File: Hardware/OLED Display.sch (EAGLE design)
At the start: 16 parts, among them J1 SM04B-SRSS-TB, J2 SM04B-SRSS-TB, U1 QG-2832TLBFG02, U2 APX803

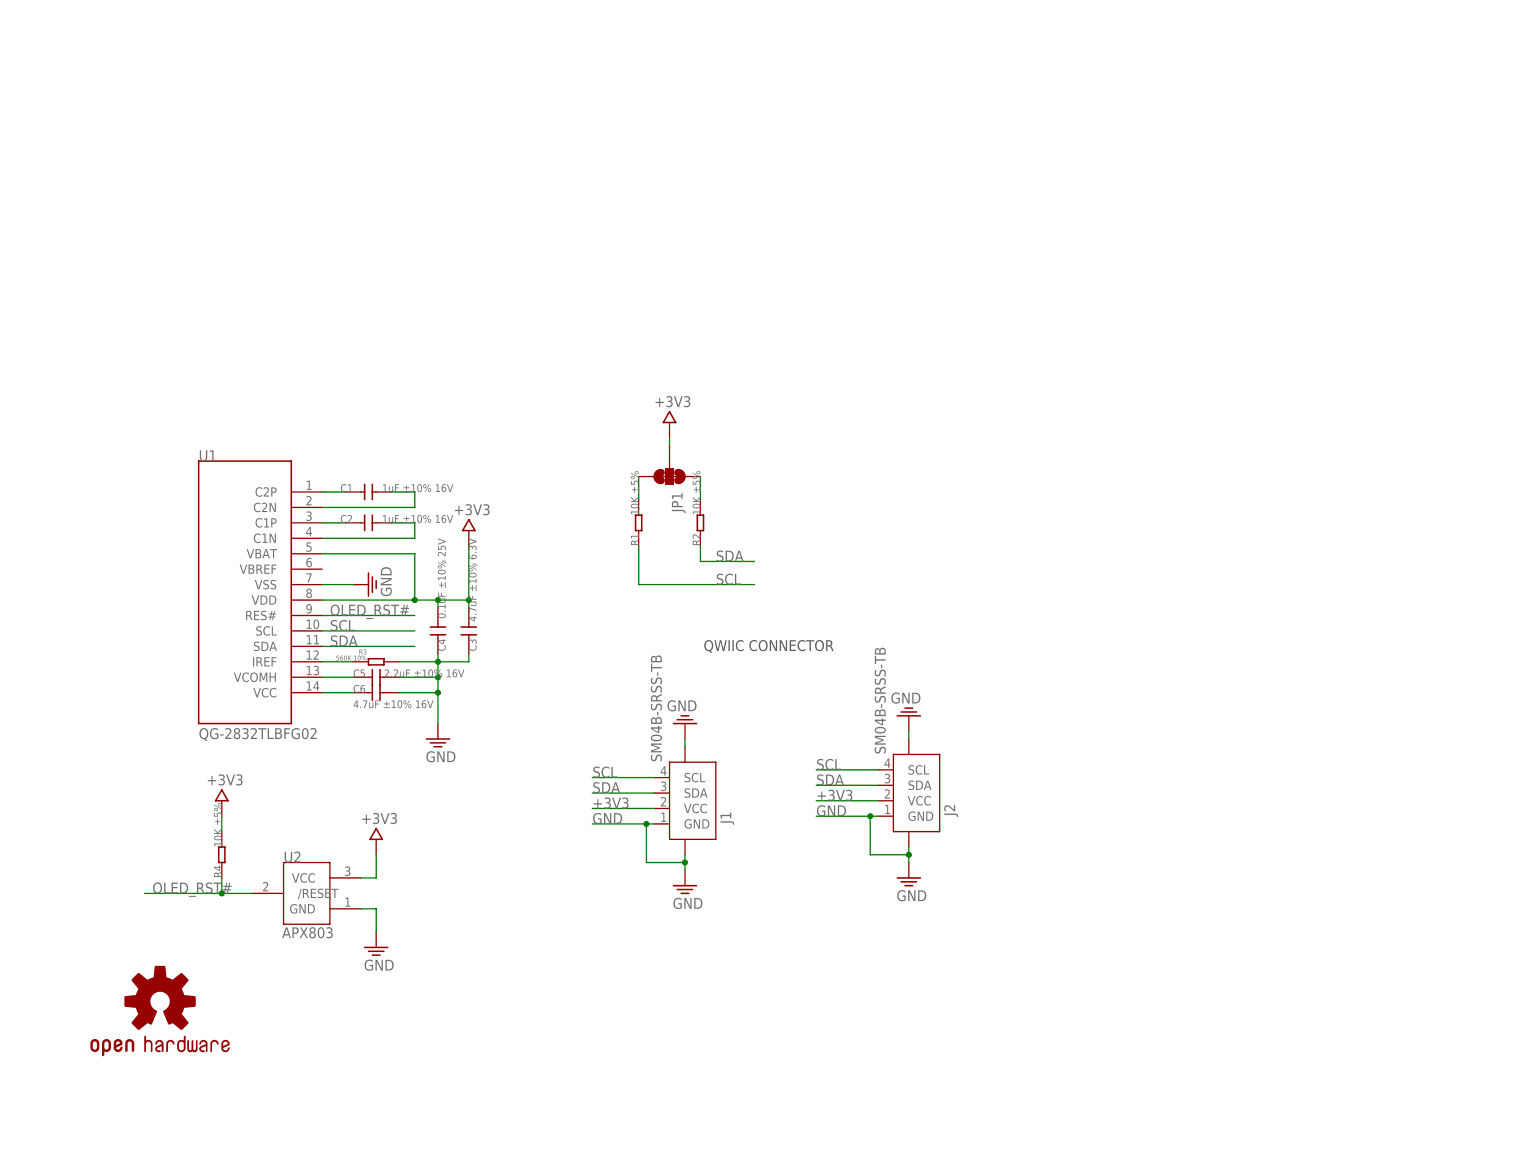
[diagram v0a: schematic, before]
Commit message: Replaces parts not in the SparkFun Eagle Libraries, adds logos, moves qwiic connectors and standoffs
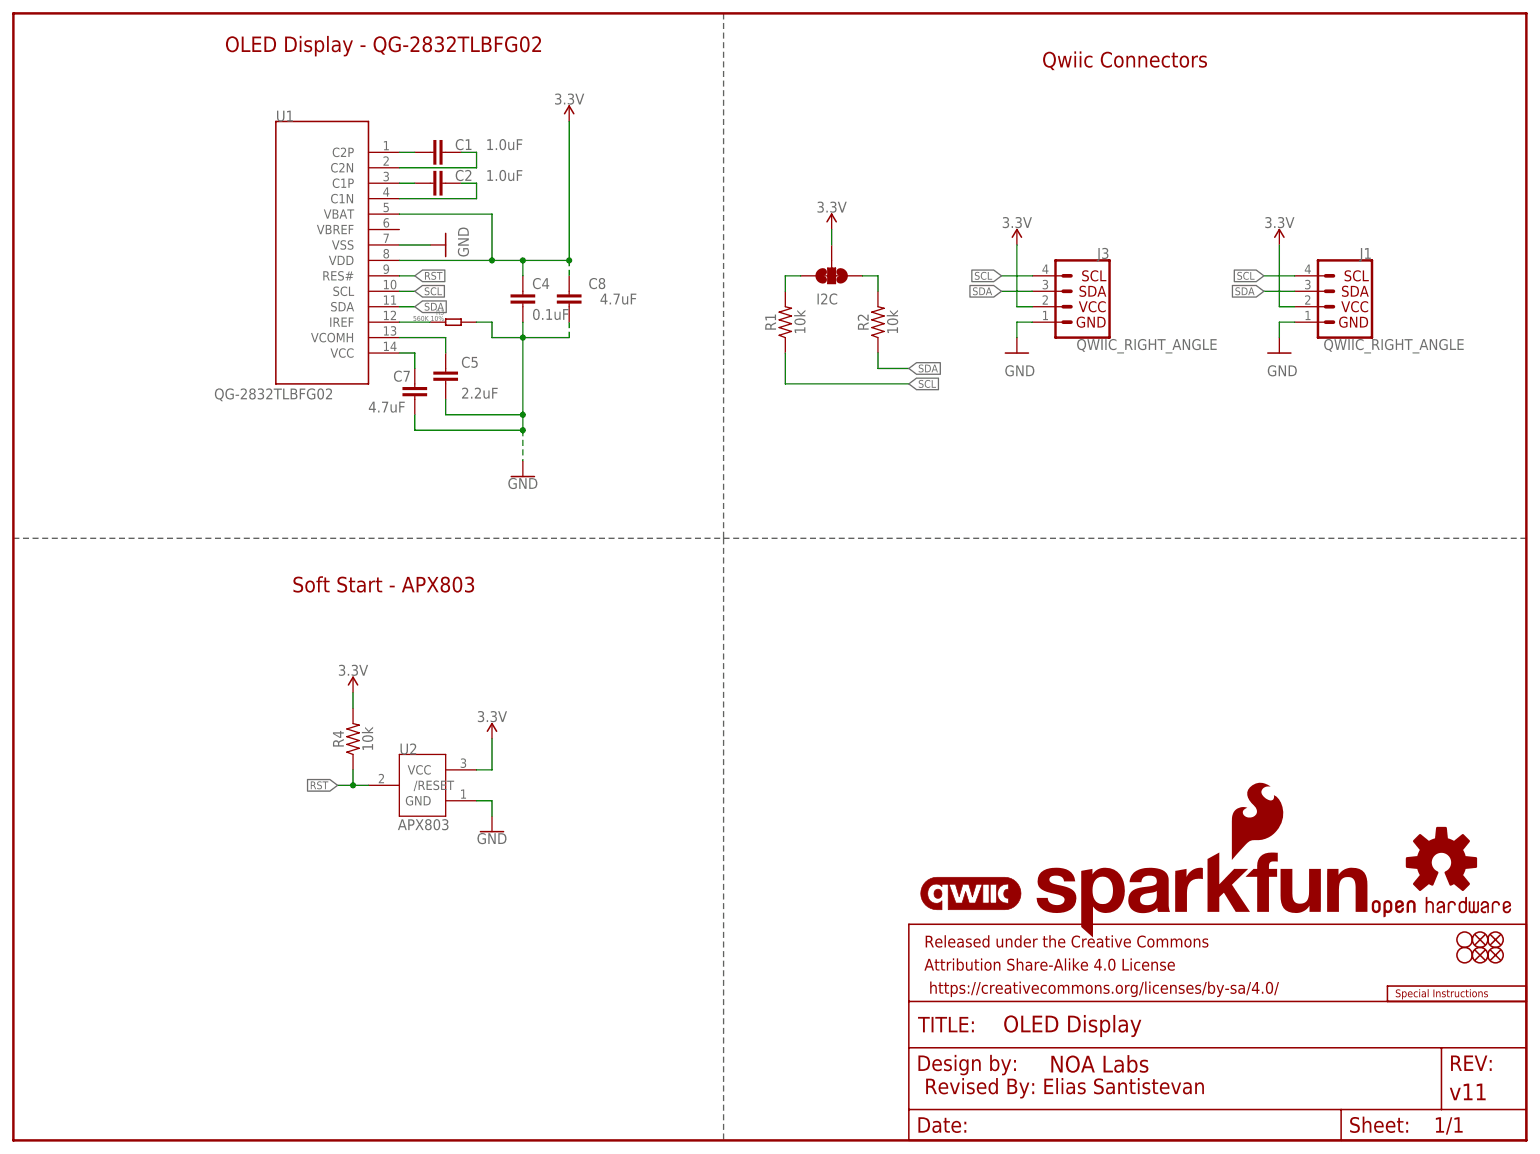
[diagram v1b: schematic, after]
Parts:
- removed C3: 4.7uF ±10% 6.3V, Discrete:C-0603
- removed C6: 4.7uF ±10% 16V, Discrete:C-0603
- removed J2: SM04B-SRSS-TB, Connector:JST-SH-4P-1.0
- removed JP1: SMT-JUMPER_3_2-NC_TRACE, NOA-Jumpers:SMT-JUMPER_3_2-NC_TRACE
- added C7, C8: 4.7uF, SparkFun-Capacitors:4.7UF-0603-6.3V-(10%)
- added FD1, FD2, FD3, FD4: FIDUCIAL1X2, SparkFun-Aesthetics:FIDUCIAL1X2
- added FRAME2: FRAME-LETTER, SparkFun-Aesthetics:FRAME-LETTER
- added H1, H2: STAND-OFFTIGHT, SparkFun-Hardware:STAND-OFFTIGHT
- added I2C: SMT-JUMPER_3_2-NC_TRACE, NOA-Jumpers:SMT-JUMPER_3_2-NC_TRACE
- added J3: QWIIC_RIGHT_ANGLE, SparkFun-Connectors:QWIIC_CONNECTORJS-1MM
- added LOGO1: SFE_LOGO_NAME_FLAME.2_INCH, SparkFun-Aesthetics:SFE_LOGO_NAME_FLAME.2_INCH
- added LOGO3: QWIIC_LOGO_4MM, SparkFun-Aesthetics:QWIIC_LOGO_4MM
- added LOGO4: SPECIAL_INSTRUCTIONS-ORDERING, SparkFun-Aesthetics:SPECIAL_INSTRUCTIONS-ORDERING
- C1, C2: value 1uF ±10% 16V -> 1.0uF; device Discrete:C-0603 -> SparkFun-Capacitors:1.0UF-0603-16V-10%
- C4: value 0.1uF ±10% 25V -> 0.1uF; device Discrete:C-0603 -> SparkFun-Capacitors:0.1UF-0603-25V-(+80/-20%)
- C5: value 2.2uF ±10% 16V -> 2.2uF; device Discrete:C-0603 -> SparkFun-Capacitors:2.2UF-0603-10V-20%
- J1: value SM04B-SRSS-TB -> QWIIC_RIGHT_ANGLE; device Connector:JST-SH-4P-1.0 -> SparkFun-Connectors:QWIIC_CONNECTORJS-1MM
- R1, R2, R4: value 10K ±5% -> 10k; device Discrete:R-0603 -> SparkFun-Resistors:10KOHM-0603-1/10W-1%
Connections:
- net OLED_RST# renamed RST
- removed net +3V3: C3.1, C4.1, J1.VCC, J2.VCC, JP1.2, R4.2, U1.VBAT, U1.VDD, U2.VCC
- new net 3.3V: C4.1, C8.2, I2C.2, J1.2, J3.2, R4.2, U1.VBAT, U1.VDD, U2.VCC
- net GND: now also C7.1, C8.1, J1.1, J3.1; no longer C3.2, C6.2, J1.5, J1.6, J1.GND, J2.5, J2.6, J2.GND
- net N$5: now also I2C.3; no longer JP1.3
- net N$7: now also C7.2; no longer C6.1
- net N$8: now also I2C.1; no longer JP1.1
- net SCL: now also J1.4, J3.4; no longer J1.SCL, J2.SCL
- net SDA: now also J1.3, J3.3; no longer J1.SDA, J2.SDA
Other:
- note added: "OLED Display - QG-2832TLBFG02"
- note added: "Qwiic Connectors"
- note added: "Revised By: Elias Santistevan"
- note added: "Soft Start - APX803"
- note removed: "QWIIC CONNECTOR"
- moved on the sheet: R3, U1, U2

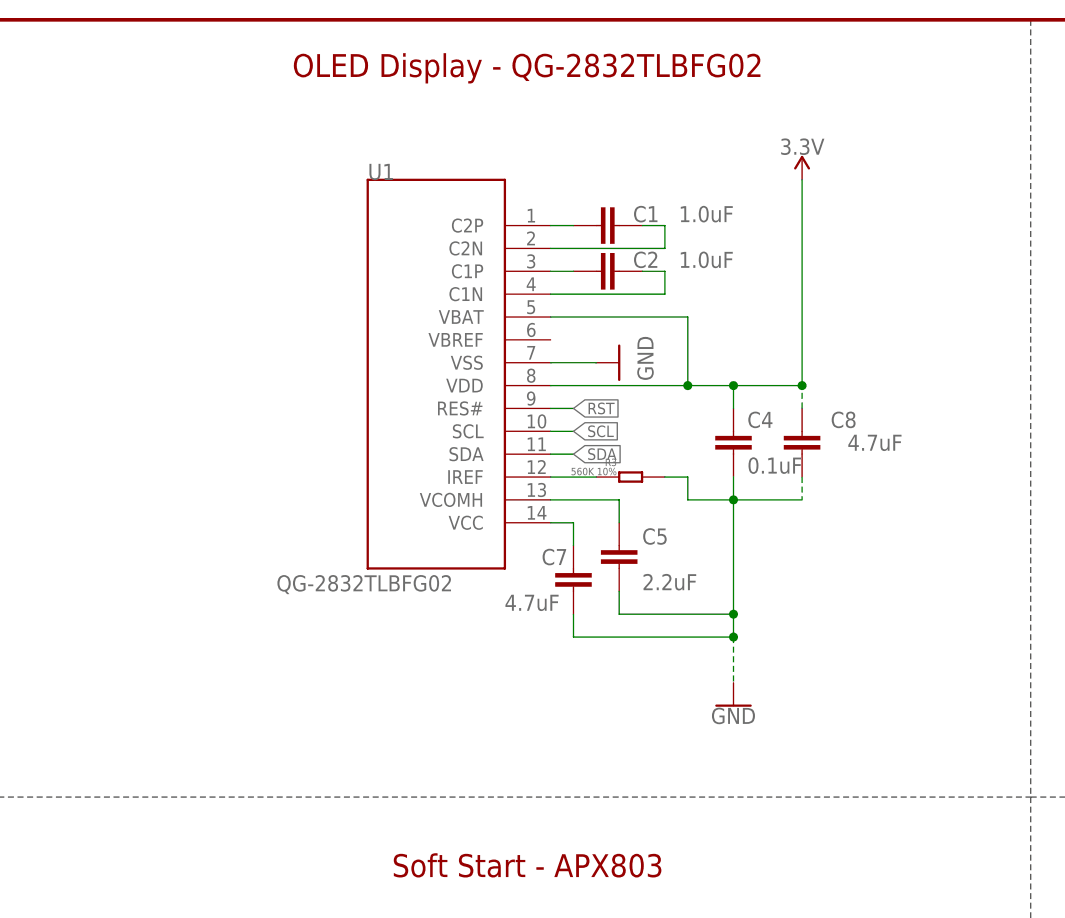
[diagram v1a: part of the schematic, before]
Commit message: Replaces more parts
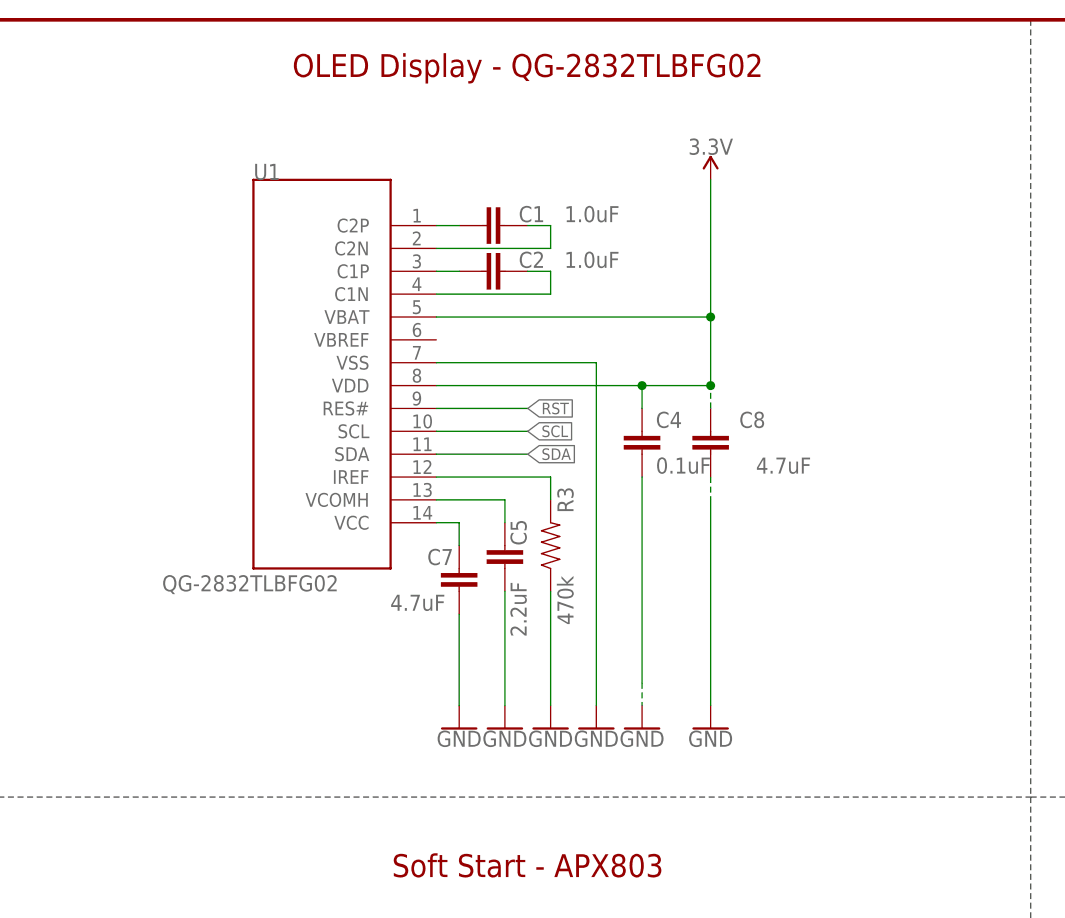
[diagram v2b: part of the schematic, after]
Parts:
- R3: value 560K 10% -> 470k; device Discrete:R-0603 -> SparkFun-Resistors:470KOHM
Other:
- moved on the sheet: C1, C2, C4, C5, C7, C8, U1

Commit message: Changes soft start circuit to RC circuit
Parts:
- removed U2: APX803, IC:APX803
- added C3: 1.0uF, SparkFun-Capacitors:1.0UF-0603-16V-10%
- R1, R2: value 10k -> 4.7k; device SparkFun-Resistors:10KOHM-0603-1/10W-1% -> SparkFun-Resistors:4.7KOHM-0603-1/10W-1%
- R4: value 10k -> 100k; device SparkFun-Resistors:10KOHM-0603-1/10W-1% -> SparkFun-Resistors:100KOHM-0603-1/10W-1%
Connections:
- net 3.3V: no longer U2.VCC
- net GND: now also C3.2; no longer U2.GND
- net RST: now also C3.1; no longer U2./RESET
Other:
- note added: "100ms Delayed Startup"
- note added: "Soft Start Circuit"
- note removed: "Soft Start - APX803"
- moved on the sheet: R4
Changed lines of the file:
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@@
 <setting verticaltext="up"/>
 </settings>
-<grid distance="0.1" unitdist="inch" unit="inch" style="lines" multiple="1" display="yes" altdistance="0.01" altunitdist="inch" altunit="inch"/>
+<grid distance="0.1" unitdist="inch" unit="inch" style="lines" multiple="1" display="no" altdistance="0.01" altunitdist="inch" altunit="inch"/>
 <layers>
 <layer number="1" name="Top" color="4" fill="1" visible="no" active="no"/>
@@
 <part name="C2" library="SparkFun-Capacitors" deviceset="1.0UF" device="-0603-16V-10%" value="1.0uF"/>
 <part name="C4" library="SparkFun-Capacitors" deviceset="0.1UF" device="-0603-25V-(+80/-20%)" value="0.1uF"/>
-<part name="R1" library="SparkFun-Resistors" deviceset="10KOHM" device="-0603-1/10W-1%" value="10k"/>
-<part name="R2" library="SparkFun-Resistors" deviceset="10KOHM" device="-0603-1/10W-1%" value="10k"/>
+<part name="R1" library="SparkFun-Resistors" deviceset="4.7KOHM" device="-0603-1/10W-1%" value="4.7k"/>
+<part name="R2" library="SparkFun-Resistors" deviceset="4.7KOHM" device="-0603-1/10W-1%" value="4.7k"/>
 <part name="R3" library="SparkFun-Resistors" deviceset="470KOHM" device="" value="470k"/>
 <part name="C5" library="SparkFun-Capacitors" deviceset="2.2UF" device="-0603-10V-20%" value="2.2uF"/>
-<part name="U2" library="IC" deviceset="APX803" device=""/>
 <part name="GND8" library="SparkFun-PowerSymbols" deviceset="GND" device=""/>
 <part name="GND9" library="SparkFun-PowerSymbols" deviceset="GND" device=""/>
@@
 <part name="SUPPLY4" library="SparkFun-PowerSymbols" deviceset="3.3V" device=""/>
 <part name="SUPPLY5" library="SparkFun-PowerSymbols" deviceset="3.3V" device=""/>
-<part name="SUPPLY6" library="SparkFun-PowerSymbols" deviceset="3.3V" device=""/>
 <part name="J3" library="SparkFun-Connectors" deviceset="QWIIC_CONNECTOR" device="JS-1MM" value="QWIIC_RIGHT_ANGLE"/>
 <part name="J1" library="SparkFun-Connectors" deviceset="QWIIC_CONNECTOR" device="JS-1MM" value="QWIIC_RIGHT_ANGLE"/>
-<part name="GND3" library="SparkFun-PowerSymbols" deviceset="GND" device=""/>
-<part name="R4" library="SparkFun-Resistors" deviceset="10KOHM" device="-0603-1/10W-1%" value="10k"/>
+<part name="R4" library="SparkFun-Resistors" deviceset="100KOHM" device="-0603-1/10W-1%" value="100k"/>
 <part name="LOGO4" library="SparkFun-Aesthetics" deviceset="SPECIAL_INSTRUCTIONS" device="-ORDERING"/>
 <part name="GND4" library="SparkFun-PowerSymbols" deviceset="GND" device=""/>
@@
 <part name="GND7" library="SparkFun-PowerSymbols" deviceset="GND" device=""/>
 <part name="GND2" library="SparkFun-PowerSymbols" deviceset="GND" device=""/>
+<part name="C3" library="SparkFun-Capacitors" deviceset="1.0UF" device="-0603-16V-10%" value="1.0uF"/>
+<part name="GND3" library="SparkFun-PowerSymbols" deviceset="GND" device=""/>
 </parts>
 <sheets>
@@
 <text x="182.88" y="177.8" size="2.54" layer="94" font="vector" align="center">Qwiic Connectors</text>
 <text x="60.96" y="180.34" size="2.54" layer="94" font="vector" align="center">OLED Display - QG-2832TLBFG02</text>
-<text x="60.96" y="91.44" size="2.54" layer="94" font="vector" align="center">Soft Start - APX803</text>
+<text x="60.96" y="91.44" size="2.54" layer="94" font="vector" align="center">Soft Start Circuit</text>
+<text x="76.2" y="58.42" size="1.27" layer="97" font="vector" align="center">100ms Delayed Startup </text>
 </plain>
 <instances>
@@
 <attribute name="NAME" x="60.833" y="127" size="1.778" layer="95" font="vector" rot="R90"/>
 <attribute name="VALUE" x="60.833" y="116.84" size="1.778" layer="96" font="vector" rot="R90"/>
-</instance>
-<instance part="U2" gate="G$1" x="67.31" y="58.42" smashed="yes">
-<attribute name="NAME" x="63.5" y="63.5" size="1.778" layer="95"/>
-<attribute name="VALUE" x="63.246" y="51.054" size="1.778" layer="96"/>
 </instance>
 <instance part="GND8" gate="1" x="165.1" y="129.54" smashed="yes">
@@
 <attribute name="VALUE" x="165.1" y="150.114" size="1.778" layer="96" font="vector" align="bottom-center"/>
 </instance>
-<instance part="SUPPLY5" gate="G$1" x="55.88" y="73.66" smashed="yes">
-<attribute name="VALUE" x="55.88" y="76.454" size="1.778" layer="96" font="vector" align="bottom-center"/>
-</instance>
-<instance part="SUPPLY6" gate="G$1" x="78.74" y="66.04" smashed="yes">
-<attribute name="VALUE" x="78.74" y="68.834" size="1.778" layer="96" font="vector" align="bottom-center"/>
+<instance part="SUPPLY5" gate="G$1" x="60.96" y="73.66" smashed="yes">
+<attribute name="VALUE" x="60.96" y="76.454" size="1.778" layer="96" font="vector" align="bottom-center"/>
 </instance>
 <instance part="J3" gate="J1" x="175.26" y="137.16" smashed="yes" rot="MR0">
@@
 <attribute name="NAME" x="223.52" y="145.034" size="1.778" layer="95" font="vector" rot="MR0"/>
 </instance>
-<instance part="GND3" gate="1" x="78.74" y="50.8" smashed="yes">
-<attribute name="VALUE" x="78.74" y="50.546" size="1.778" layer="96" font="vector" align="top-center"/>
-</instance>
-<instance part="R4" gate="G$1" x="55.88" y="66.04" smashed="yes" rot="R90">
-<attribute name="NAME" x="54.356" y="66.04" size="1.778" layer="95" font="vector" rot="R90" align="bottom-center"/>
-<attribute name="VALUE" x="57.404" y="66.04" size="1.778" layer="96" font="vector" rot="R90" align="top-center"/>
+<instance part="R4" gate="G$1" x="60.96" y="66.04" smashed="yes" rot="R90">
+<attribute name="NAME" x="59.436" y="66.04" size="1.778" layer="95" font="vector" rot="R90" align="bottom-center"/>
+<attribute name="VALUE" x="62.484" y="66.04" size="1.778" layer="96" font="vector" rot="R90" align="top-center"/>
 </instance>
 <instance part="LOGO4" gate="G$1" x="226.06" y="22.86" smashed="yes"/>
@@
 <instance part="GND2" gate="1" x="68.58" y="106.68" smashed="yes">
 <attribute name="VALUE" x="68.58" y="106.426" size="1.778" layer="96" font="vector" align="top-center"/>
+</instance>
+<instance part="C3" gate="G$1" x="60.96" y="50.8" smashed="yes">
+<attribute name="NAME" x="62.484" y="53.721" size="1.778" layer="95" font="vector"/>
+<attribute name="VALUE" x="62.484" y="48.641" size="1.778" layer="96" font="vector"/>
+</instance>
+<instance part="GND3" gate="1" x="60.96" y="43.18" smashed="yes">
+<attribute name="VALUE" x="60.96" y="42.926" size="1.778" layer="96" font="vector" align="top-center"/>
 </instance>
 </instances>
@@
 </segment>
 <segment>
-<pinref part="U2" gate="G$1" pin="GND"/>
-<wire x1="76.2" y1="55.88" x2="78.74" y2="55.88" width="0.1524" layer="91"/>
-<pinref part="GND3" gate="1" pin="GND"/>
-<wire x1="78.74" y1="55.88" x2="78.74" y2="53.34" width="0.1524" layer="91"/>
-</segment>
-<segment>
 <pinref part="U1" gate="G$1" pin="VSS"/>
 <wire x1="50.8" y1="147.32" x2="68.58" y2="147.32" width="0.1524" layer="91"/>
@@
 <pinref part="GND2" gate="1" pin="GND"/>
 </segment>
+<segment>
+<pinref part="C3" gate="G$1" pin="2"/>
+<wire x1="60.96" y1="48.26" x2="60.96" y2="45.72" width="0.1524" layer="91"/>
+<pinref part="GND3" gate="1" pin="GND"/>
+</segment>
 </net>
 <net name="SCL" class="0">
@@
 </segment>
 <segment>
-<pinref part="U2" gate="G$1" pin="/RESET"/>
 <pinref part="R4" gate="G$1" pin="1"/>
-<wire x1="55.88" y1="58.42" x2="58.42" y2="58.42" width="0.1524" layer="91"/>
-<wire x1="55.88" y1="60.96" x2="55.88" y2="58.42" width="0.1524" layer="91"/>
-<label x="53.34" y="58.42" size="1.27" layer="95" font="vector" rot="R180" xref="yes"/>
-<wire x1="53.34" y1="58.42" x2="55.88" y2="58.42" width="0.1524" layer="91"/>
-<junction x="55.88" y="58.42"/>
+<wire x1="60.96" y1="60.96" x2="60.96" y2="58.42" width="0.1524" layer="91"/>
+<label x="58.42" y="58.42" size="1.27" layer="95" font="vector" rot="R180" xref="yes"/>
+<wire x1="58.42" y1="58.42" x2="60.96" y2="58.42" width="0.1524" layer="91"/>
+<junction x="60.96" y="58.42"/>
+<pinref part="C3" gate="G$1" pin="1"/>
+<wire x1="60.96" y1="55.88" x2="60.96" y2="58.42" width="0.1524" layer="91"/>
 </segment>
 </net>
@@
 </segment>
 <segment>
-<pinref part="U2" gate="G$1" pin="VCC"/>
-<wire x1="76.2" y1="60.96" x2="78.74" y2="60.96" width="0.1524" layer="91"/>
-<pinref part="SUPPLY6" gate="G$1" pin="3.3V"/>
-<wire x1="78.74" y1="60.96" x2="78.74" y2="66.04" width="0.1524" layer="91"/>
-</segment>
-<segment>
 <pinref part="R4" gate="G$1" pin="2"/>
-<wire x1="55.88" y1="71.12" x2="55.88" y2="73.66" width="0.1524" layer="91"/>
+<wire x1="60.96" y1="71.12" x2="60.96" y2="73.66" width="0.1524" layer="91"/>
 <pinref part="SUPPLY5" gate="G$1" pin="3.3V"/>
 </segment>
